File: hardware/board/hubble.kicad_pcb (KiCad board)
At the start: 2 copper layers, 100 x 100 mm, 118 parts, among them J1 POWER, J2 SWD, J3 USB_B_Receptacle, J4 EXT, J5 Left, J6 Right, J7 Bottom, J8 EXT, J9 EXT, SW1 POWER, SW2 Reset, U1 LD1117-3.3, U10 OPA4197, U11 MCP6004, U2 LM4040-10, U3 LM4040-10, U4 MUX509, U5 ATSAMD51J20A-M, U6 AD5685R?RUZ, U7 MUX509, U8 MUX509, U9 MUX509, Y1 32.768 kHz

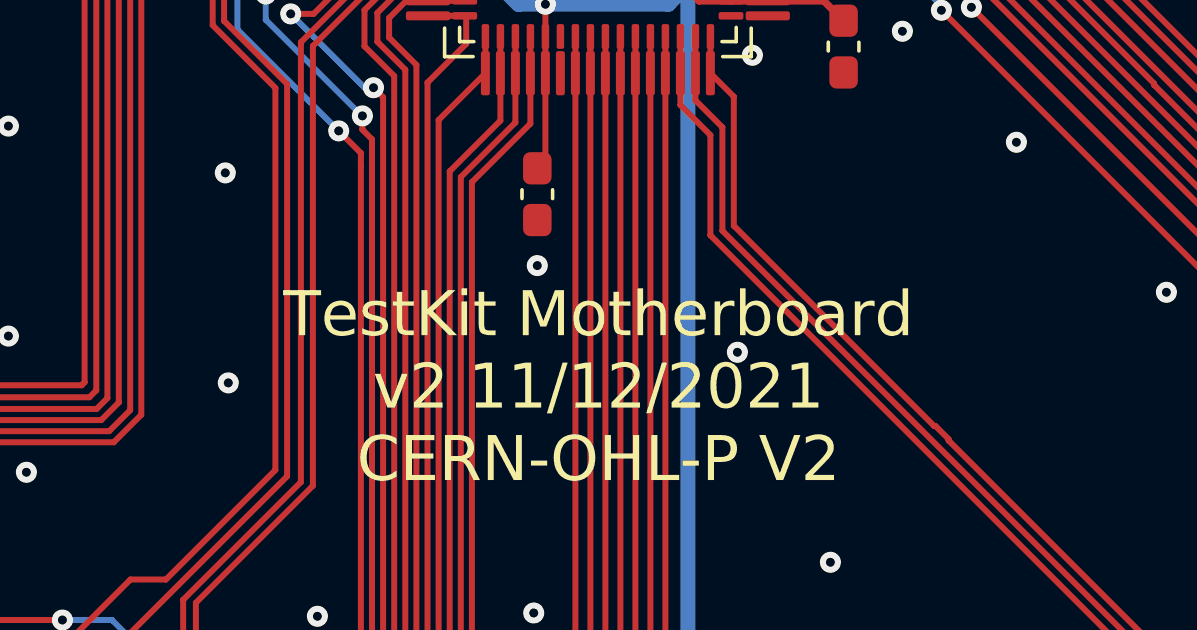
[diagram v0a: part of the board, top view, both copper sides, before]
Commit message: Rename Testkit board to Hubble
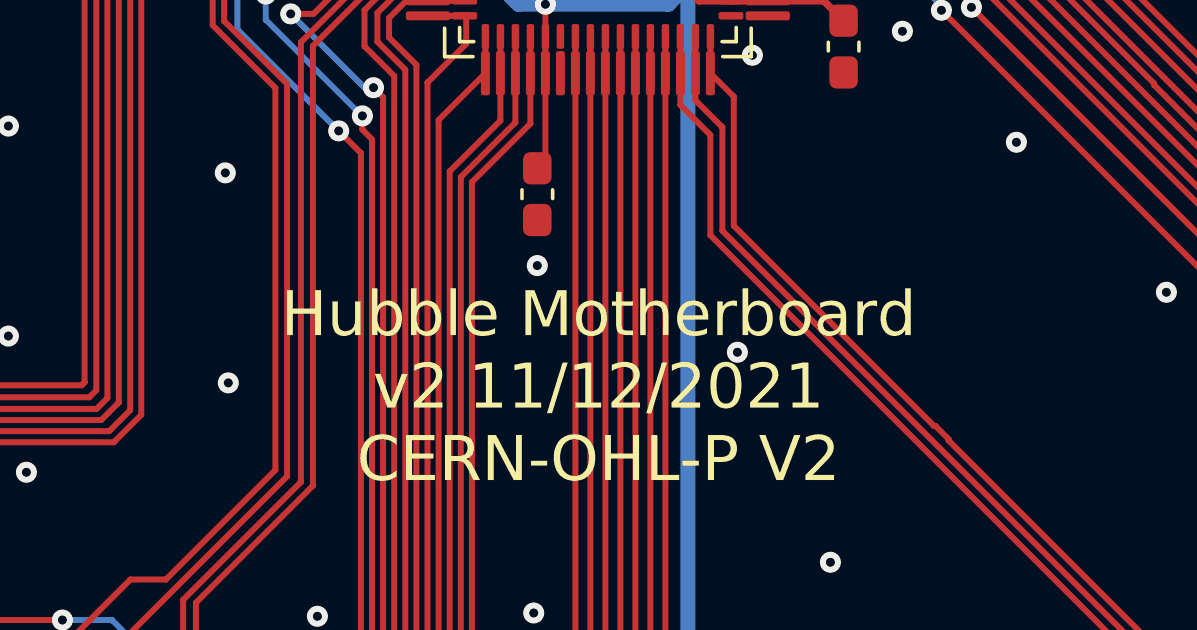
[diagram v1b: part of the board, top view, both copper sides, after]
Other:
- board text added: "Hubble Motherboard v2 11/12/2021 CERN-OHL-P V2"
- board text removed: "TestKit Motherboard v2 11/12/2021 CERN-OHL-P V2"
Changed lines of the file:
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@@
   (page A4)
   (title_block
-    (title "TestKit Motherboard")
+    (title "Hubble Motherboard")
     (date 2021-10-31)
     (rev v1)
@@
     (effects (font (size 0.7 0.7) (thickness 0.15)))
   )
-  (gr_text "TestKit Motherboard\nv2 11/12/2021\nCERN-OHL-P V2" (at 126.07 100.15) (layer F.SilkS)
+  (gr_text "Hubble Motherboard\nv2 11/12/2021\nCERN-OHL-P V2" (at 126.07 100.15) (layer F.SilkS)
     (effects (font (size 1.5 1.5) (thickness 0.2)))
   )
